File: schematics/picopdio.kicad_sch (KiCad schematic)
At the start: 14 parts, among them J2 SWD+UART, J3 AudioJack3, SW1 Builtin Front Power Switch, SW2 Builtin Rear Power Switch, U1 MXA-10C_IR_Adapter_Main_Board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, U2 Pico, U3 Adafruit_VS1053B_Breakout, U4 W5500_Lite USR-ES1, U5 MCP23017_SP, U6 SparkFun_SX1509_Expander, U7 Pololu_2808

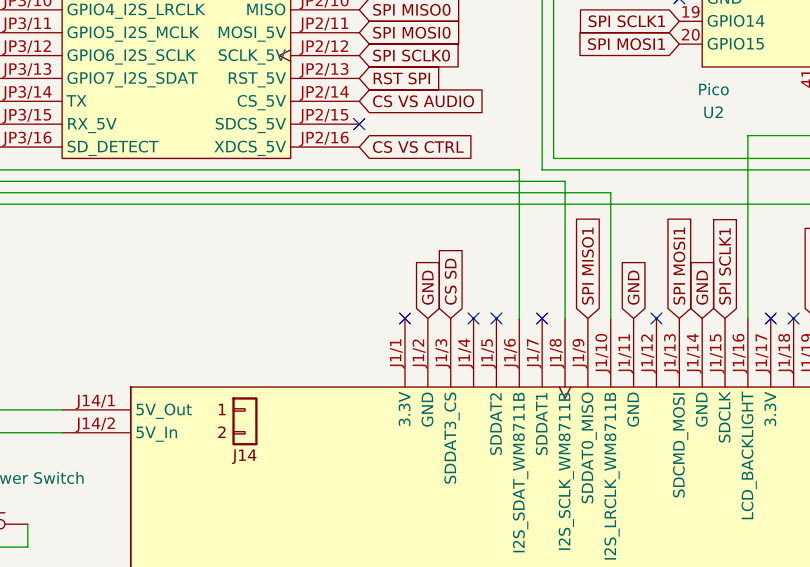
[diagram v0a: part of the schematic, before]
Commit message: Improve power supply
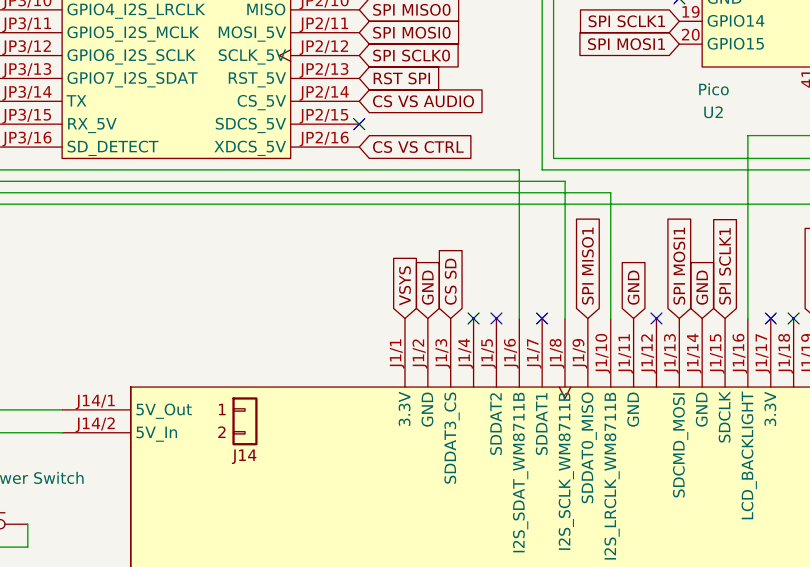
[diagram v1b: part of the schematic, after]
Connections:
- net VSYS: now also U1.J1/1 (3.3V)
- no-connect marks 118 -> 117
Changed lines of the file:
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@@
   (no_connect (at 179.07 46.99))
   (no_connect (at 156.21 100.33))
-  (no_connect (at 148.59 100.33))
   (no_connect (at 189.23 100.33))
   (no_connect (at 176.53 100.33))
@@
       (effects (font (size 1.27 1.27)) (justify left) hide)
     )
+  )
+  (global_label "VSYS" (shape input) (at 148.59 100.33 90) (fields_autoplaced)
+    (effects (font (size 1.27 1.27)) (justify left))
+    (property "Intersheet References" "${INTERSHEET_REFS}" (id 0) (at 148.5106 93.3207 90)
+      (effects (font (size 1.27 1.27)) (justify left) hide)
+    )

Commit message: wip
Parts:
- removed J3: AudioJack3, symbol Connector:AudioJack3
- removed R2: 10k, symbol Device:R
- removed R3: 100, symbol Device:R
- removed SW1: Builtin Front Power Switch, symbol Switch:SW_Push
- removed SW2: Builtin Rear Power Switch, symbol Switch:SW_SPST
- removed U4: W5500_Lite USR-ES1, symbol picopdio:W5500_Lite USR-ES1
- removed U5: MCP23017_SP, Package_DIP:DIP-28_W7.62mm, symbol Interface_Expansion:MCP23017_SP
- added J1, J2: JST XH, symbol Connector_Generic:Conn_01x02
- added J3: Pico USB, symbol Connector_Generic:Conn_01x05
- added U4: ~, symbol picopdio:MAX4053
- added U5: 74HC137, symbol 74xx:74HC137
- added U8: SRC4192, Package_SO:SSOP-28_5.3x10.2mm_P0.65mm, symbol picopdio:SRC4192
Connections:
- net CS ETH is gone; now on an unnamed net: U2.29 (GPIO22)
- net 3V3: now also U5.16 (VCC), U5.6 (E2), U8.10 (IFMT0), U8.16 (OWL1), U8.17 (OWL0), U8.19 (OFMT0), U8.22 (V_{DD}), U8.7 (V_{IO}); no longer R1.1
- net CS SD: now also U4.11 (ADDC), U5.12 (~{Y3}); no longer U2.17 (GPIO13)
- net CS VS AUDIO: now also U5.13 (~{Y2}); no longer U2.6 (GPIO4)
- net CS VS CTRL: now also U5.14 (~{Y1}); no longer U2.7 (GPIO5)
- net GND: now also R1.2, U1.J2/30 (USB_ETH_PWR_~{EN}), U4.6 (INH), U4.7 (V-), U4.8 (GND), U5.3 (A2), U5.4 (~{LE}), U5.5 (~{E1}), U5.8 (GND), U8.1 (LGRP), U8.11 (IFMT1), U8.12 (IFMT2), U8.14 (MUTE), U8.18 (OFMT1), U8.20 (TDMI), U8.21 (DGND), U8.26 (MODE0), U8.27 (MODE1), U8.28 (MODE2), U8.8 (DGND), U8.9 (BYPAS)
- net SPI MISO0: now also U4.14 (COMC); no longer U3.JP2/10 (MISO)
- net SPI MOSI0: now also U1.J1/13 (SDCMD_MOSI)
- net SPI SCLK0: now also U1.J1/15 (SDCLK)
- net RG188: now reaches U3.JP3/11 (GPIO5_I2S_MCLK)
- net RG188: now also U8.2 (RCKI)
- net at J2.1 (Pin_1): now also U2.J2/3 (SWDIO); no longer U2.43 (SWDIO)
- net at J2.3 (Pin_3): now also U2.J2/2 (GND); no longer U2.42 (GND)
- net at J2.5 (Pin_5): now also U2.J2/1 (SWCLK); no longer U2.41 (SWCLK)
- net at U1.J1/10 (I2S_LRCLK_WM8711B): now also U8.24 (LRCKO); no longer U3.JP3/10 (GPIO4_I2S_LRCLK)
- net at U1.J1/16 (LCD_BACKLIGHT): no longer U2.22 (GPIO17)
- net at U1.J1/6 (I2S_SDAT_WM8711B): now also U8.23 (SDOUT); no longer U3.JP3/13 (GPIO7_I2S_SDAT)
- net at U1.J1/8 (I2S_SCLK_WM8711B): now also U8.25 (BCKO); no longer U3.JP3/12 (GPIO6_I2S_SCLK)
- net at U7.8 (VOUT): now also R1.1, J1.1 (Pin_1), U4.10 (ADDB), U4.9 (ADDA); no longer U1.J14/2 (5V_In)
- net at U1.J2/10 (SD_Card_Detect): now also U6.J3/8 (GPIO2)
- net at U1.J2/19 (Knob_Low_Bit): no longer U2.15 (GPIO11)
- net at U1.J2/21 (Knob_High_Bit): now also U2.31 (GPIO26_ADC0); no longer U2.14 (GPIO10)
- net at U1.J2/24 (ONBOARD_USB_DN): now also J3.2 (Pin_2)
- net at U1.J2/26 (ONBOARD_USB_DP): now also J3.3 (Pin_3)
- net LCD_~{POWER}: now reaches U1.J3/10 (LCD_Power_Act.Low)
- net LCD_~{POWER}: now also U6.J4/16 (GPIO14)
- net D3: now reaches U1.J3/11 (LCD_ST7565_8080_D3)
- net D3: now also U2.15 (GPIO11)
- net LCD_~{CS}: now reaches U1.J3/12 (LCD_ST7565_8080_~{CS1})
- net LCD_~{CS}: now also U6.J4/8 (GPIO11)
- net D2: now reaches U1.J3/13 (LCD_ST7565_8080_D2)
- net D2: now also U2.14 (GPIO10)
- net LCD_RESET: now reaches U1.J3/14 (LCD_ST7565_/RES)
- net LCD_RESET: now also U6.J4/14 (GPIO13)
- net D1: now reaches U1.J3/15 (LCD_ST7565_8080_D1)
- net D1: now also U2.12 (GPIO9)
- net LCD_DC: now reaches U1.J3/16 (LCD_ST7565_8080_A0_~{RS}|DC)
- net LCD_DC: now also U2.10 (GPIO7)
- net D0: now reaches U1.J3/17 (LCD_ST7565_8080_D0)
- net D0: now also U2.11 (GPIO8)
- net LCD_~{WR}|EN: now reaches U1.J3/18 (LCD_ST7565_8080_~{WR})
- net LCD_~{WR}|EN: now also U2.9 (GPIO6)
- net LCD_~{RD}: now reaches U1.J3/20 (LCD_ST7565_8080_~{RD})
- net LCD_~{RD}: now also U6.J4/12 (GPIO12)
- net D7: now reaches U1.J3/3 (LCD_ST7565_8080_D7)
- net D7: now also U2.20 (GPIO15)
- net D6: now reaches U1.J3/5 (LCD_ST7565_8080_D6)
- net D6: now also U2.19 (GPIO14)
- net D5: now reaches U1.J3/7 (LCD_ST7565_8080_D5)
- net D5: now also U2.17 (GPIO13)
- net D4: now reaches U1.J3/9 (LCD_ST7565_8080_D4)
- net D4: now also U2.16 (GPIO12)
- net DREQ: now reaches U3.JP2/6 (DREQ)
- net DREQ: now also U2.22 (GPIO17); no longer U2.9 (GPIO6)
- net at U7.12 (B): now also U4.2 (NCB)
- net at U7.13 (A): now also U4.5 (NCA)
- net ~{SRC_RDY}: now reaches U6.J3/20 (GPIO7)
- net ~{SRC_RDY}: now also U8.15 (~{RDY})
- net LCD_PWM: now reaches U6.J4/18 (GPIO15)
- net at U7.1 (VIN): now also J2.1 (Pin_1), U4.16 (V+)
- net I2C SCL1: no longer names the net of U2.32 (GPIO27_ADC1)
- removed net I2C SDA1: R1.2, U2.31 (GPIO26_ADC0)
- net RST I2C renamed RST CORE1
- net RST SPI renamed RST CORE0
- net RST CORE0: now also U8.13 (~{RST})
- net SPI MISO1 renamed SPI MISO SD
- net SPI MISO SD: now also U4.13 (NOC); no longer U2.16 (GPIO12)
- removed net SPI MOSI1: U1.J1/13 (SDCMD_MOSI), U2.20 (GPIO15)
- removed net SPI SCLK1: U1.J1/15 (SDCLK), U2.19 (GPIO14)
- net Shielded: no longer names the net of U1.U3/1 (WM8711B_XTI/MCLK)
- new net: U2.6 (GPIO4), U5.1 (A0)
- new net: U2.7 (GPIO5), U5.2 (A1)
- new net: U3.JP3/10 (GPIO4_I2S_LRCLK), U8.6 (LRCKI)
- new net: U3.JP3/12 (GPIO6_I2S_SCLK), U8.5 (BCKI)
- new net: U3.JP3/13 (GPIO7_I2S_SDAT), U8.4 (SDIN)
- new net: J1.2 (Pin_2), J2.2 (Pin_2)
- new net KEY_COL2: U4.15 (COMB)
- new net KEY_COL2_GPIO: U4.1 (NOB)
- new net KEY_ROW1: U4.4 (COMA)
- new net KEY_ROW1_GPIO: U4.3 (NOA)
- new net SPI MISO N: U3.JP2/10 (MISO), U4.12 (NCC)
- no-connect marks 117 -> 107
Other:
- note added: "Mainboard Power"
- note added: "Rear Power Switch"
- note added: "USB_DM"
- note added: "USB_DP"
- note added: "USB_GND"
- note added: "USB_SHIELD"
- note added: "USB_VBUS"
- moved on the sheet: J2, U6, U7
